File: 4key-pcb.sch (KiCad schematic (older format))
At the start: 1 part

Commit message: finished eeschema
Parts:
- added C?: 1uf, symbol Device:C_Small
- added C? (x3): 0.1uf, symbol Device:C_Small
- added C?: 10uf, symbol Device:C_Small
- added C? (x2): 22pf, symbol Device:C_Small
- added R? (x2): 10k, symbol Device:R_Small
- added R? (x2): 22, symbol Device:R_Small
- added SW?: SW_Push, symbol Switch:SW_Push
- added Y?: Crystal_GND24_Small, symbol Device:Crystal_GND24_Small
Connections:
- net +5V: now also U?.7 (VBUS), C?.1, C?.1, C?.1, C?.1, R?.1
- net GND: now also C?.2, C?.2, C?.2, C?.2, C?.2, C?.2, R?.1, SW?.1, Y?.2, Y?.4
- net at U?.13 (~RESET): now also R?.2, SW?.2
- net at U?.16 (XTAL2): now also C?.1, Y?.3
- net at U?.17 (XTAL1): now also C?.1, Y?.1
- net at U?.3 (D-): now also R?.1
- net at U?.33 (~HWB~/PE2): now also R?.2
- net at U?.4 (D+): now also R?.1
- new net D+: R?.2
- new net D-: R?.2

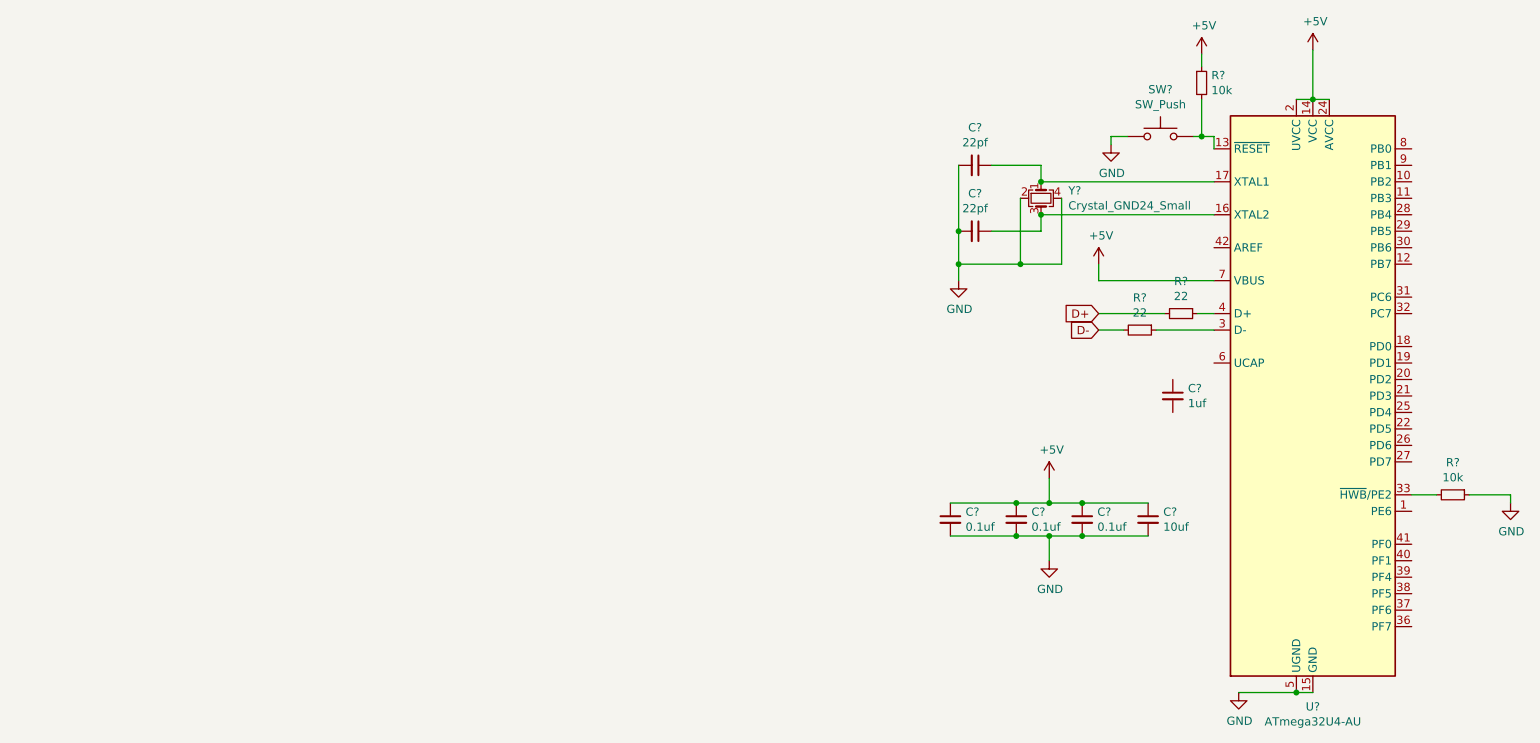
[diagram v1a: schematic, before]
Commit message: finished usb, switches and applied footprints
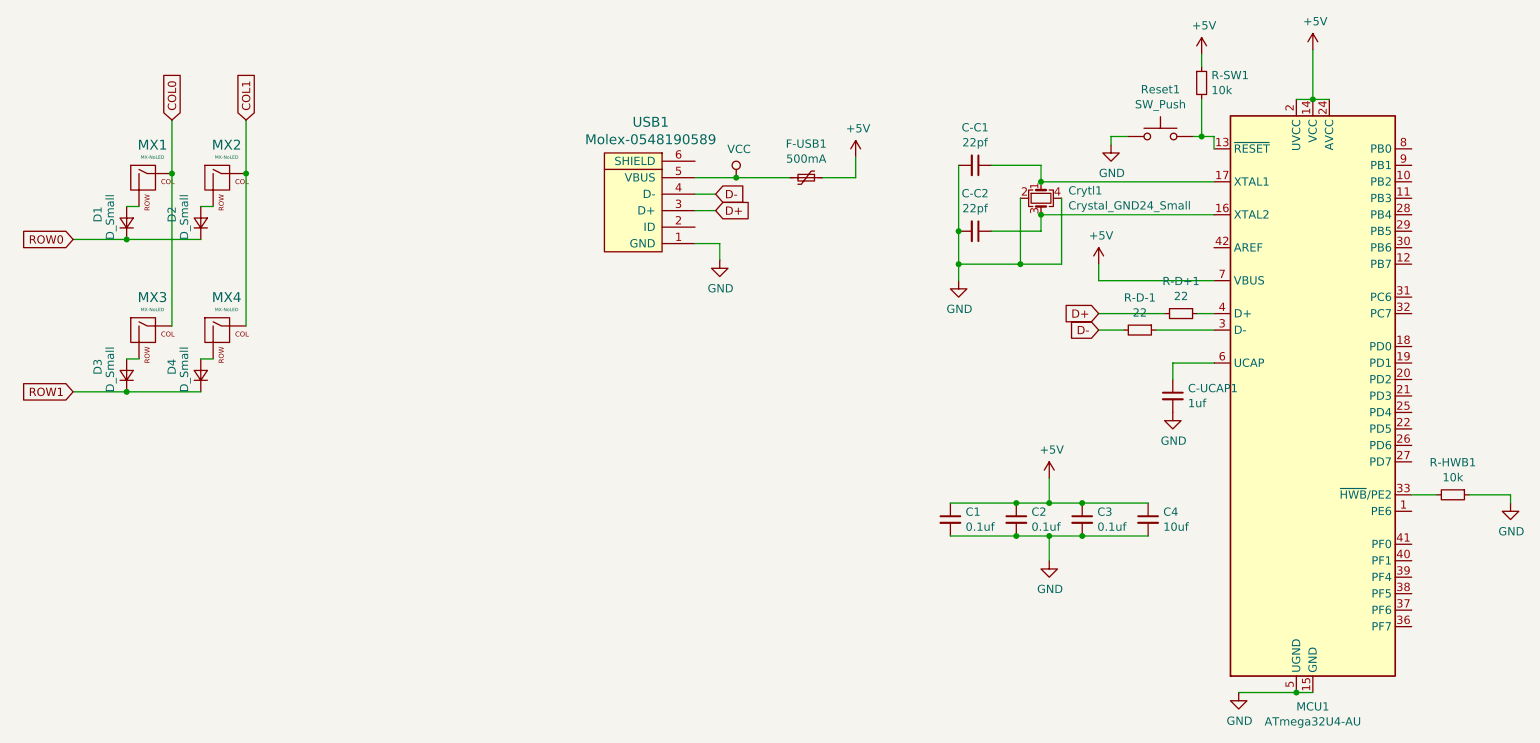
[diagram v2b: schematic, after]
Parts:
- added D1, D2, D3, D4: D_Small, Diode_SMD:D_SOD-123, symbol Device:D_Small
- added F-USB1: 500mA, Fuse:Fuse_1206_3216Metric, symbol Device:Polyfuse_Small
- added MX1, MX2, MX3, MX4: MX-NoLED, MX_Alps_Hybrid:MX-1U-NoLED, symbol MX_Alps_Hybrid:MX-NoLED
- added USB1: Molex-0548190589, random-keyboard-parts:Molex-0548190589, symbol random-keyboard-parts:Molex-0548190589
- C-C1, C-C2, C-UCAP1, C1, C2, C3, C4: renamed from C?; footprint (none) -> Capacitor_THT:C_Rect_L29.0mm_W13.8mm_P27.50mm_MKT
- Crytl1: renamed from Y?; footprint (none) -> Crystal:Crystal_SMD_3225-4Pin_3.2x2.5mm
- R-D+1, R-D-1, R-HWB1, R-SW1: renamed from R?; footprint (none) -> Resistor_SMD:R_0805_2012Metric
- Reset1: renamed from SW?; footprint (none) -> random-keyboard-parts:SKQG-1155865
- gave numbers to parts that had none: 1
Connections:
- net +5V: now also F-USB1.1
- net D+: now also USB1.3 (D+)
- net D-: now also USB1.4 (D-)
- net GND: now also C-UCAP1.2, USB1.1 (GND)
- net at MCU1.6 (UCAP): now also C-UCAP1.1
- new net: D1.2 (A), MX1.2 (ROW)
- new net: D2.2 (A), MX2.2 (ROW)
- new net: D3.2 (A), MX3.2 (ROW)
- new net: D4.2 (A), MX4.2 (ROW)
- new net COL0: MX1.1 (COL), MX3.1 (COL)
- new net COL1: MX2.1 (COL), MX4.1 (COL)
- new net ROW0: D1.1 (K), D2.1 (K)
- new net ROW1: D3.1 (K), D4.1 (K)
- new net VCC: F-USB1.2, USB1.5 (VBUS)
